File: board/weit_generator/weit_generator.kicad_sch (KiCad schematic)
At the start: 21 parts, among them U1 AVR32DA28x-xSO, U2 TL074

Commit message: .
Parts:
- removed R10, R11, R12, R13, R14, R15, R16: 10k, symbol Device:R
- removed R17: R_Photo, symbol Device:R_Photo
- removed R2, R3, R4, R5, R6, R7, R8, R9: 20k, symbol Device:R
- removed RV1: R_Potentiometer, symbol Device:R_Potentiometer
- removed U2: TL074, symbol Amplifier_Operational:TL074
- added C1: 10U, Capacitor_SMD:C_0805_2012Metric_Pad1.18x1.45mm_HandSolder, symbol Device:C
- added C11: 100n, Capacitor_THT:C_Rect_L13.0mm_W6.0mm_P10.00mm_FKS3_FKP3_MKS4, symbol Device:C
- added C2, C3, C4: 100n, Capacitor_SMD:C_0805_2012Metric_Pad1.18x1.45mm_HandSolder, symbol Device:C
- added J1: POWER, Connector_PinHeader_2.54mm:PinHeader_1x02_P2.54mm_Vertical, symbol Connector_Generic:Conn_01x02
- added J2: PROG, Connector_PinHeader_2.54mm:PinHeader_1x03_P2.54mm_Vertical, symbol Connector_Generic:Conn_01x03
- added J3: OUTPUT, Connector_PinHeader_2.54mm:PinHeader_1x02_P2.54mm_Vertical, symbol Connector_Generic:Conn_01x02
- added R2: R_Photo, Connector_PinHeader_2.54mm:PinHeader_1x02_P2.54mm_Vertical, symbol Device:R_Photo
- added U1: MCP6004, Package_SO:SOIC-14_3.9x8.7mm_P1.27mm, symbol Amplifier_Operational:MCP6004
- added X1: SG-5032CCN, Oscillator:Oscillator_SMD_SeikoEpson_SG8002LB-4Pin_5.0x3.2mm_HandSoldering, symbol Oscillator:SG-5032CCN
- D1: footprint (none) -> LED_THT:LED_D5.0mm_Horizontal_O3.81mm_Z3.0mm
- R1: value 20k -> 5k; footprint (none) -> Resistor_THT:R_Axial_DIN0207_L6.3mm_D2.5mm_P2.54mm_Vertical
- renumbered U1 to U2
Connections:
- net GND: now also D1.1 (K), C1.2, C2.2, C3.2, C4.2, J1.2 (Pin_2), J2.1 (Pin_1), J3.2 (Pin_2), R2.1, U1.11 (V-), X1.2 (GND); no longer R1.1
- net BUS6: now reaches U2.12 (PD6)
- net Autogain/OUT: now reaches D1.2 (A)
- net BUS0: now reaches U2.6 (PD0)
- net BUS4: now reaches U2.10 (PD4)
- net BUS5: now reaches U2.11 (PD5)
- net BUS7: now reaches U2.13 (VREFA/PD7)
- net +3V0: now reaches U2.14 (AVDD)
- net +3V0: now also U2.20 (VDD), C1.1, C2.1, C3.1, C4.1, J1.1 (Pin_1), U1.4 (V+), X1.4 (Vcc)
- net at U2.18 (~{RESET}/PF6): now also J2.3 (Pin_3)
- net at U2.19 (UPDI): now also J2.2 (Pin_2)
- net at U2.22 (PA0): now also X1.3 (OUT)
- net BUS1: now reaches U2.7 (PD1)
- net BUS2: now reaches U2.8 (PD2)
- net BUS3: now reaches U2.9 (PD3)
- net Output Filter/IN: now reaches R1.2
- net Output Filter/IN: now also R2.2
- new net OUTPUT: C11.2, J3.1 (Pin_1)
- new net Output Filter/OUT: C11.1
- new net R-2R DAC/OUT: R1.1
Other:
- added sheet Autogain (autogain.kicad_sch)
- added sheet Output Filter (filter.kicad_sch)
- added sheet R-2R DAC (dac.kicad_sch)
- note added: "Crude voltage-controlled-resistor, works as an attenuator"
- moved on the sheet: U2

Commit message: .
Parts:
- removed C4: 100n, Capacitor_SMD:C_0805_2012Metric_Pad1.18x1.45mm_HandSolder, symbol Device:C
- removed X1: SG-5032CCN, Oscillator:Oscillator_SMD_SeikoEpson_SG8002LB-4Pin_5.0x3.2mm_HandSoldering, symbol Oscillator:SG-5032CCN
- added C13: 100n, Capacitor_SMD:C_0805_2012Metric_Pad1.18x1.45mm_HandSolder, symbol Device:C
- added TP1: TestPoint, TestPoint:TestPoint_Pad_D3.0mm, symbol Connector:TestPoint
- added U4: LMV321, Package_TO_SOT_SMD:SOT-23-5_HandSoldering, symbol Amplifier_Operational:LM321
- added X1: SG-5032CAN, Oscillator:Oscillator_SMD_SeikoEpson_SG8002LB-4Pin_5.0x3.2mm, symbol Oscillator:SG-5032CAN
- U1: footprint Package_SO:SOIC-14_3.9x8.7mm_P1.27mm -> Package_DIP:DIP-14_W7.62mm_Socket_LongPads
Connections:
- net +3V0: now also C13.1, U4.5 (V+), X1.4 (VCC)
- net GND: now also C13.2, U4.2 (V-), X1.2 (GND)
- net Output Filter/OUT: now also U4.1 (+); no longer C11.1
- net R-2R DAC/OUT: now also TP1.1
- net at U2.22 (PA0): now also X1.3 (OUT)
- new net: C11.1, U4.3 (-), U4.4
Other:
- note added: "Output driver (TBD)"
- moved on the sheet: C11, J3

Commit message: hopefully repaired instability
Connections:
- net +3V0: now also D1.2 (A)
- net Autogain/OUT: now also D1.1 (K); no longer D1.2 (A)
- net GND: no longer D1.1 (K)
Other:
- added sheet Voltage reference (vref.kicad_sch)
- sheet Autogain ports: added Vref; removed none
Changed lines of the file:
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@@
+    (stroke (width 0) (type default))
+  )
+  (wire (pts (xy 220.345 139.065) (xy 217.805 139.065))
     (stroke (width 0) (type default))
   )
@@
     (stroke (width 0) (type default))
   )
+  (wire (pts (xy 220.345 116.205) (xy 220.345 139.065))
+    (stroke (width 0) (type default))
+  )
   (wire (pts (xy 240.03 88.9) (xy 240.03 99.695))
     (stroke (width 0) (type default))
@@
     (stroke (width 0) (type default))
   )
-  (wire (pts (xy 183.515 89.535) (xy 183.515 109.855))
-    (stroke (width 0) (type default))
-  )
   (wire (pts (xy 216.535 109.855) (xy 253.365 109.855))
     (stroke (width 0) (type default))
@@
     (stroke (width 0) (type default))
   )
-  (wire (pts (xy 183.515 109.855) (xy 193.675 109.855))
+  (wire (pts (xy 173.355 109.855) (xy 193.675 109.855))
     (stroke (width 0) (type default))
   )
@@
     (stroke (width 0) (type default))
   )
+  (wire (pts (xy 173.355 97.155) (xy 173.355 109.855))
+    (stroke (width 0) (type default))
+  )
   (wire (pts (xy 253.365 88.9) (xy 253.365 92.71))
     (stroke (width 0) (type default))
@@
     (stroke (width 0) (type default))
   )
+  (wire (pts (xy 216.535 116.205) (xy 220.345 116.205))
+    (stroke (width 0) (type default))
+  )
   (wire (pts (xy 99.06 54.61) (xy 101.6 54.61))
-    (stroke (width 0) (type default))
-  )
-  (wire (pts (xy 173.355 89.535) (xy 183.515 89.535))
     (stroke (width 0) (type default))
   )
@@
         (path "/b85c55a9-e1f6-4dbf-a795-73634abf8d52"
           (reference "X1") (unit 1)
+        )
+      )
+    )
+  )
+  (symbol (lib_id "power:+3V0") (at 173.355 89.535 0) (unit 1)
+    (in_bom yes) (on_board yes) (dnp no) (fields_autoplaced)
+    (property "Reference" "#PWR019" (at 173.355 93.345 0)
+      (effects (font (size 1.27 1.27)) hide)
+    )
+    (property "Value" "+3V0" (at 173.355 85.725 0)
+      (effects (font (size 1.27 1.27)))
+    )
+    (property "Footprint" "" (at 173.355 89.535 0)
+      (effects (font (size 1.27 1.27)) hide)
+    )
+    (property "Datasheet" "" (at 173.355 89.535 0)
+      (effects (font (size 1.27 1.27)) hide)
+    )
+    (pin "1")
+    (instances
+      (project "weit_generator"
+        (path "/b85c55a9-e1f6-4dbf-a795-73634abf8d52"
+          (reference "#PWR019") (unit 1)
         )
       )
@@
     )
   )
-  (symbol (lib_id "power:GND") (at 173.355 97.155 0) (unit 1)
-    (in_bom yes) (on_board yes) (dnp no) (fields_autoplaced)
-    (property "Reference" "#PWR019" (at 173.355 103.505 0)
-      (effects (font (size 1.27 1.27)) hide)
-    )
-    (property "Value" "GND" (at 173.355 102.235 0)
-      (effects (font (size 1.27 1.27)))
-    )
-    (property "Footprint" "" (at 173.355 97.155 0)
-      (effects (font (size 1.27 1.27)) hide)
-    )
-    (property "Datasheet" "" (at 173.355 97.155 0)
-      (effects (font (size 1.27 1.27)) hide)
-    )
-    (pin "1")
-    (instances
-      (project "weit_generator"
-        (path "/b85c55a9-e1f6-4dbf-a795-73634abf8d52"
-          (reference "#PWR019") (unit 1)
-        )
-        (path "/b85c55a9-e1f6-4dbf-a795-73634abf8d52/97b440c2-49e0-43c1-8dbd-070a3fa32fe0"
-          (reference "#PWR?") (unit 1)
-        )
-      )
-    )
-  )
   (symbol (lib_id "Amplifier_Operational:MCP6004") (at 90.17 165.1 0) (unit 5)
     (in_bom yes) (on_board yes) (dnp no) (fields_autoplaced)
@@
     )
   )
-  (sheet (at 193.675 106.68) (size 22.86 6.35) (fields_autoplaced)
+  (sheet (at 193.675 106.68) (size 22.86 14.605) (fields_autoplaced)
     (stroke (width 0.1524) (type solid))
     (fill (color 0 0 0 0.0000))
@@
       (effects (font (size 1.27 1.27)) (justify left bottom))
     )
-    (property "Sheetfile" "autogain.kicad_sch" (at 193.675 113.6146 0)
+    (property "Sheetfile" "autogain.kicad_sch" (at 193.675 121.8696 0)
       (effects (font (size 1.27 1.27)) (justify left top))
     )
@@
     (pin "OUT" input (at 193.675 109.855 180)
       (effects (font (size 1.27 1.27)) (justify left))
+    )
+    (pin "Vref" input (at 216.535 116.205 0)
+      (effects (font (size 1.27 1.27)) (justify right))
     )
     (instances
@@
       )
     )
+  )
+  (sheet (at 192.405 133.35) (size 25.4 10.16) (fields_autoplaced)
+    (stroke (width 0.1524) (type solid))
+    (fill (color 0 0 0 0.0000))
+    (property "Sheetname" "Voltage reference" (at 192.405 132.6384 0)
+      (effects (font (size 1.27 1.27)) (justify left bottom))
+    )
+    (property "Sheetfile" "vref.kicad_sch" (at 192.405 144.0946 0)
+      (effects (font (size 1.27 1.27)) (justify left top))
+    )
+    (property "Field2" "" (at 192.405 133.35 0)
+      (effects (font (size 1.27 1.27)) hide)
+    )
+    (pin "05V" input (at 217.805 139.065 0)
+      (effects (font (size 1.27 1.27)) (justify right))
+    )
+    (instances
+      (project "weit_generator"
+        (path "/b85c55a9-e1f6-4dbf-a795-73634abf8d52" (page "5"))
+      )
+    )

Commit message: New layout
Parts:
- removed C1: 10U, Capacitor_SMD:C_0805_2012Metric_Pad1.18x1.45mm_HandSolder, symbol Device:C
- removed C3: 100n, Capacitor_SMD:C_0805_2012Metric_Pad1.18x1.45mm_HandSolder, symbol Device:C
- added C1: 100u, Capacitor_THT:CP_Radial_D6.3mm_P2.50mm, symbol Device:C_Polarized
- added C2: 1u, Capacitor_THT:C_Rect_L7.2mm_W4.5mm_P5.00mm_FKS2_FKP2_MKS2_MKP2, symbol Device:C
- added C4: 100n, Capacitor_THT:C_Rect_L7.2mm_W2.5mm_P5.00mm_FKS2_FKP2_MKS2_MKP2, symbol Device:C
- added C6: 100n, Capacitor_THT:C_Rect_L13.0mm_W6.0mm_P10.00mm_FKS3_FKP3_MKS4, symbol Device:C
- added R1: 1k, Resistor_SMD:R_0805_2012Metric_Pad1.20x1.40mm_HandSolder, symbol Device:R
- added unit 2 of U1
- added U?: LM4041L, Package_TO_SOT_THT:TO-92_Inline, symbol Reference_Voltage:LM4041LP-ADJ
- C3: renamed from C2; footprint Capacitor_SMD:C_0805_2012Metric_Pad1.18x1.45mm_HandSolder -> Capacitor_THT:C_Rect_L7.2mm_W2.5mm_P5.00mm_FKS2_FKP2_MKS2_MKP2
- C5: renamed from C13; footprint Capacitor_SMD:C_0805_2012Metric_Pad1.18x1.45mm_HandSolder -> Capacitor_THT:C_Rect_L7.2mm_W2.5mm_P5.00mm_FKS2_FKP2_MKS2_MKP2
- C7: renamed from C11; Dielectric (none) -> Polisteryne
- U1: footprint Package_DIP:DIP-14_W7.62mm_Socket_LongPads -> Package_DIP:DIP-14_W7.62mm_Socket
- renumbered R1 to R2, R2 to R3
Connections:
- net +3V0: now also C1.1, C4.1, R1.1, U1.5 (+)
- net GND: now also C1.2, C2.2, C4.2, U1.6 (-), U?.3 (A)
- net at C7.1, U4.3 (-), U4.4: now also C6.1
- net OUTPUT renamed Autogain/IN
- net Autogain/IN: now also C6.2
- new net +1V2: C2.1, R1.2, U?.2 (K)
- no-connect marks 0 -> 2
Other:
- removed sheet Voltage reference
- sheet Autogain ports: added none; removed Vref
- moved on the sheet: C7, D1, J2, J3, R2, R3, TP1, U2, U4, X1

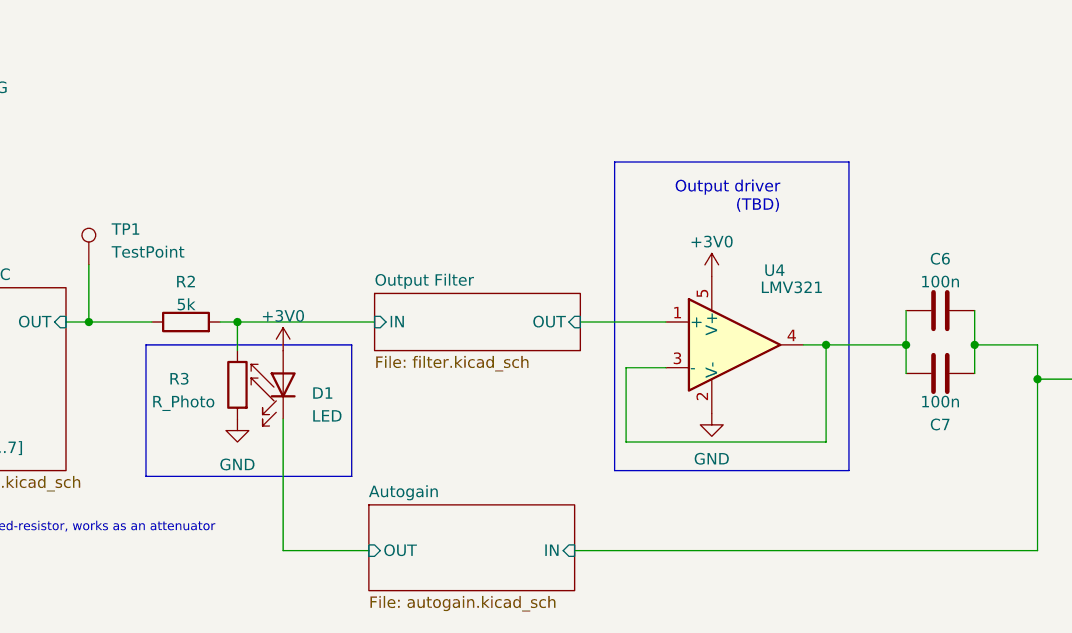
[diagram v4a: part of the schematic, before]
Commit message: finished board, added test desription and tuning to docs
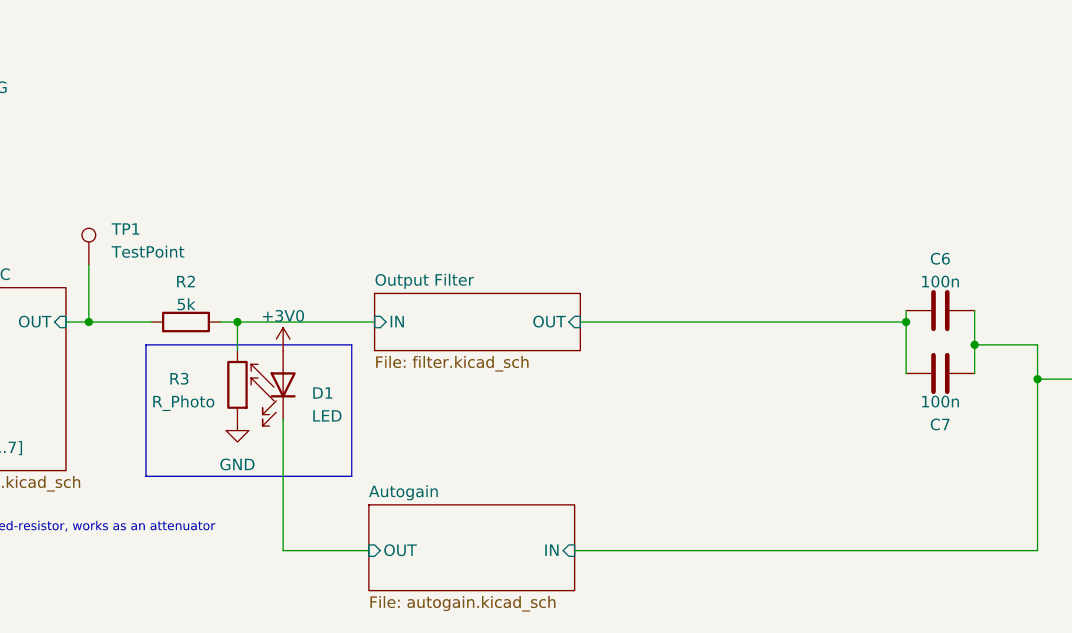
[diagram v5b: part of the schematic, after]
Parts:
- removed U4: LMV321, Package_TO_SOT_SMD:SOT-23-5_HandSoldering, symbol Amplifier_Operational:LM321
- TP1: footprint TestPoint:TestPoint_Pad_D3.0mm -> TestPoint:TestPoint_Pad_D2.0mm
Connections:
- net Output Filter/IN: now also R2.1; no longer R2.2
- net Output Filter/OUT: now also C6.1, C7.1
- net R-2R DAC/OUT: now also R2.2; no longer R2.1
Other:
- note removed: "Output driver (TBD)"
- moved on the sheet: R2
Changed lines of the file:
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@@
   (junction (at 241.935 77.47) (diameter 0) (color 0 0 0 0)
   )
-  (junction (at 227.33 73.66) (diameter 0) (color 0 0 0 0)
-  )
   (junction (at 96.52 128.905) (diameter 0) (color 0 0 0 0)
   )
-  (junction (at 218.44 73.66) (diameter 0) (color 0 0 0 0)
+  (junction (at 227.33 71.12) (diameter 0) (color 0 0 0 0)
   )
   (junction (at 107.315 128.905) (diameter 0) (color 0 0 0 0)
@@
     (stroke (width 0) (type default))
   )
-  (wire (pts (xy 191.135 71.12) (xy 200.66 71.12))
-    (stroke (width 0) (type default))
-  )
-  (wire (pts (xy 196.215 84.455) (xy 218.44 84.455))
-    (stroke (width 0) (type default))
-  )
-  (wire (pts (xy 196.215 76.2) (xy 196.215 84.455))
-    (stroke (width 0) (type default))
-  )
   (wire (pts (xy 83.185 128.905) (xy 85.725 128.905))
     (stroke (width 0) (type default))
@@
     (stroke (width 0) (type default))
   )
+  (wire (pts (xy 191.135 71.12) (xy 227.33 71.12))
+    (stroke (width 0) (type default))
+  )
   (wire (pts (xy 109.22 57.15) (xy 109.22 45.72))
     (stroke (width 0) (type default))
@@
     (stroke (width 0) (type default))
   )
-  (wire (pts (xy 218.44 73.66) (xy 218.44 84.455))
-    (stroke (width 0) (type default))
-  )
   (bus (pts (xy 113.03 77.47) (xy 113.03 80.01))
     (stroke (width 0) (type default))
@@
     (stroke (width 0) (type default))
   )
-  (wire (pts (xy 218.44 73.66) (xy 227.33 73.66))
-    (stroke (width 0) (type default))
-  )
   (wire (pts (xy 104.14 74.93) (xy 110.49 74.93))
     (stroke (width 0) (type default))
@@
     (stroke (width 0) (type default))
   )
-  (wire (pts (xy 227.33 69.85) (xy 227.33 73.66))
+  (wire (pts (xy 227.33 71.12) (xy 227.33 76.835))
     (stroke (width 0) (type default))
   )
@@
     (stroke (width 0) (type default))
   )
-  (wire (pts (xy 218.44 73.66) (xy 215.9 73.66))
-    (stroke (width 0) (type default))
-  )
   (wire (pts (xy 104.14 57.15) (xy 109.22 57.15))
     (stroke (width 0) (type default))
@@
     (stroke (width 0) (type default))
   )
-  (wire (pts (xy 200.66 76.2) (xy 196.215 76.2))
-    (stroke (width 0) (type default))
-  )
   (wire (pts (xy 133.985 71.12) (xy 136.525 71.12))
     (stroke (width 0) (type default))
@@
     (stroke (width 0) (type default))
   )
-  (wire (pts (xy 227.33 76.835) (xy 227.33 73.66))
-    (stroke (width 0) (type default))
-  )
-  (rectangle (start 194.945 53.34) (end 220.98 87.63)
+  (wire (pts (xy 227.33 69.85) (xy 227.33 71.12))
+    (stroke (width 0) (type default))
+  )
+  (rectangle (start 142.875 73.66) (end 165.735 88.265)
     (stroke (width 0) (type default))
     (fill (type none))
-  )
-  (rectangle (start 142.875 73.66) (end 165.735 88.265)
-    (stroke (width 0) (type default))
-    (fill (type none))
-  )
-  (text "Output driver\n(TBD)\n" (at 213.36 59.055 0)
-    (effects (font (size 1.27 1.27)) (justify right bottom))
   )
   (text "Crude voltage-controlled-resistor, works as an attenuator"
@@
         (path "/b85c55a9-e1f6-4dbf-a795-73634abf8d52"
           (reference "C1") (unit 1)
-        )
-      )
-    )
-  )
-  (symbol (lib_id "power:GND") (at 205.74 81.28 0) (unit 1)
-    (in_bom yes) (on_board yes) (dnp no)
-    (property "Reference" "#PWR027" (at 205.74 87.63 0)
-      (effects (font (size 1.27 1.27)) hide)
-    )
-    (property "Value" "GND" (at 205.74 86.36 0)
-      (effects (font (size 1.27 1.27)))
-    )
-    (property "Footprint" "" (at 205.74 81.28 0)
-      (effects (font (size 1.27 1.27)) hide)
-    )
-    (property "Datasheet" "" (at 205.74 81.28 0)
-      (effects (font (size 1.27 1.27)) hide)
-    )
-    (pin "1")
-    (instances
-      (project "weit_generator"
-        (path "/b85c55a9-e1f6-4dbf-a795-73634abf8d52"
-          (reference "#PWR027") (unit 1)
         )
       )
@@
     )
   )
-  (symbol (lib_id "Amplifier_Operational:LM321") (at 208.28 73.66 0) (unit 1)
-    (in_bom yes) (on_board yes) (dnp no)
-    (property "Reference" "U4" (at 212.725 65.405 0)
-      (effects (font (size 1.27 1.27)))
-    )
-    (property "Value" "LMV321" (at 214.63 67.31 0)
-      (effects (font (size 1.27 1.27)))
-    )
-    (property "Footprint" "Package_TO_SOT_SMD:SOT-23-5_HandSoldering" (at 208.28 73.66 0)
-      (effects (font (size 1.27 1.27)) hide)
-    )
-    (property "Datasheet" "http://www.ti.com/lit/ds/symlink/lm321.pdf" (at 208.28 73.66 0)
-      (effects (font (size 1.27 1.27)) hide)
-    )
-    (pin "1")
-    (pin "2")
-    (pin "3")
-    (pin "4")
-    (pin "5")
-    (instances
-      (project "weit_generator"
-        (path "/b85c55a9-e1f6-4dbf-a795-73634abf8d52"
-          (reference "U4") (unit 1)
-        )
-      )
-    )
-  )
   (symbol (lib_id "power:GND") (at 96.52 136.525 0) (unit 1)
     (in_bom yes) (on_board yes) (dnp no) (fields_autoplaced)
@@
     )
   )
-  (symbol (lib_id "power:+3V0") (at 205.74 66.04 0) (unit 1)
-    (in_bom yes) (on_board yes) (dnp no)
-    (property "Reference" "#PWR026" (at 205.74 69.85 0)
-      (effects (font (size 1.27 1.27)) hide)
-    )
-    (property "Value" "+3V0" (at 205.74 62.23 0)
-      (effects (font (size 1.27 1.27)))
-    )
-    (property "Footprint" "" (at 205.74 66.04 0)
-      (effects (font (size 1.27 1.27)) hide)
-    )
-    (property "Datasheet" "" (at 205.74 66.04 0)
-      (effects (font (size 1.27 1.27)) hide)
-    )
-    (pin "1")
-    (instances
-      (project "weit_generator"
-        (path "/b85c55a9-e1f6-4dbf-a795-73634abf8d52"
-          (reference "#PWR026") (unit 1)
-        )
-      )
-    )
-  )
   (symbol (lib_id "power:GND") (at 153.035 81.915 0) (unit 1)
     (in_bom yes) (on_board yes) (dnp no) (fields_autoplaced)
@@
       (effects (font (size 1.27 1.27)) (justify left))
     )
-    (property "Footprint" "TestPoint:TestPoint_Pad_D3.0mm" (at 141.605 64.77 0)
+    (property "Footprint" "TestPoint:TestPoint_Pad_D2.0mm" (at 141.605 64.77 0)
       (effects (font (size 1.27 1.27)) hide)
     )
@@
     )
   )
-  (symbol (lib_id "Device:R") (at 147.32 71.12 90) (unit 1)
-    (in_bom yes) (on_board yes) (dnp no) (fields_autoplaced)
+  (symbol (lib_id "Device:R") (at 147.32 71.12 270) (mirror x) (unit 1)
+    (in_bom yes) (on_board yes) (dnp no)
     (property "Reference" "R2" (at 147.32 66.675 90)
       (effects (font (size 1.27 1.27)))
